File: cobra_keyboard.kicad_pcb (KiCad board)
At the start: 2 copper layers, 298.4 x 116.8 mm, 93 parts, among them K100 DOWN, K101 UP, K102 SPACE, K103 LEFT, K104 RIGHT, K200 CTRL, K201 CS, K202 Z, K203 X, K204 C, K205 V, K206 B, K207 N, K208 M, K209 NEW M, K210 SS, K211 F4, K300 NO SCR, K301 CS LK, K302 GRAPH, K303 A, K304 S, K305 D, K306 F, K307 G, K308 H, K309 J, K310 K, K311 L, K312 ENTER, K313 F3, K400 LF, K401 TAB, K402 Q, K403 W, K404 E, K405 R, K406 T, K407 Y, K408 U, K409 I, K410 O, K411 P, K412 F2, K500 ESC, K501 PG ED, K502 1, K503 2, K504 3, K505 4, K506 5, K507 6, K508 7, K509 8, K510 9, K511 0, K512 DEL, K513 F1, T201 BC337, T210 BC337, T411 BC337, T502 BC337, T503 BC337, T506 BC337, T507 BC337, T508 BC337, T509 BC337, T510 BC337, T511 BC337

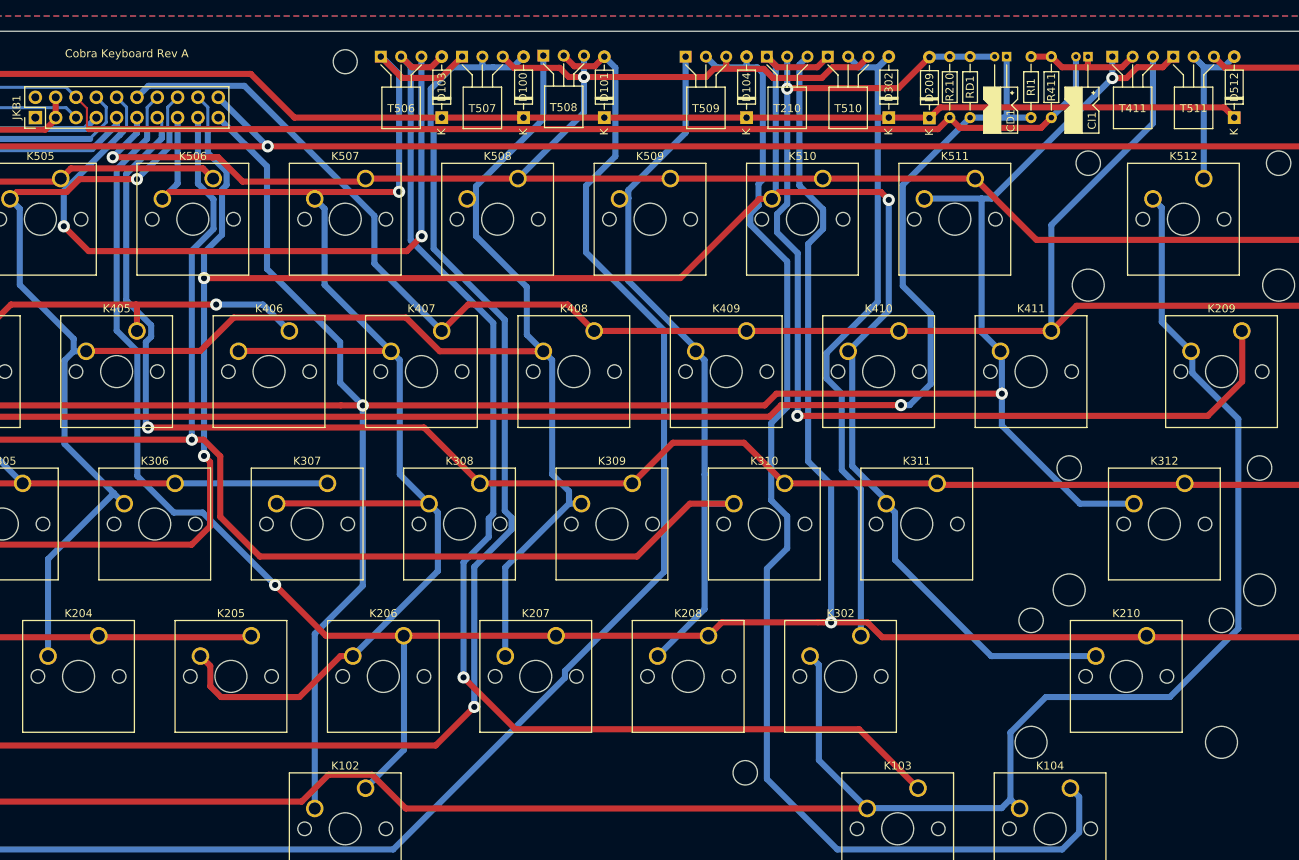
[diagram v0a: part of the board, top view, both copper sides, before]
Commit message: Swap GRAPH and NEW MODE keys
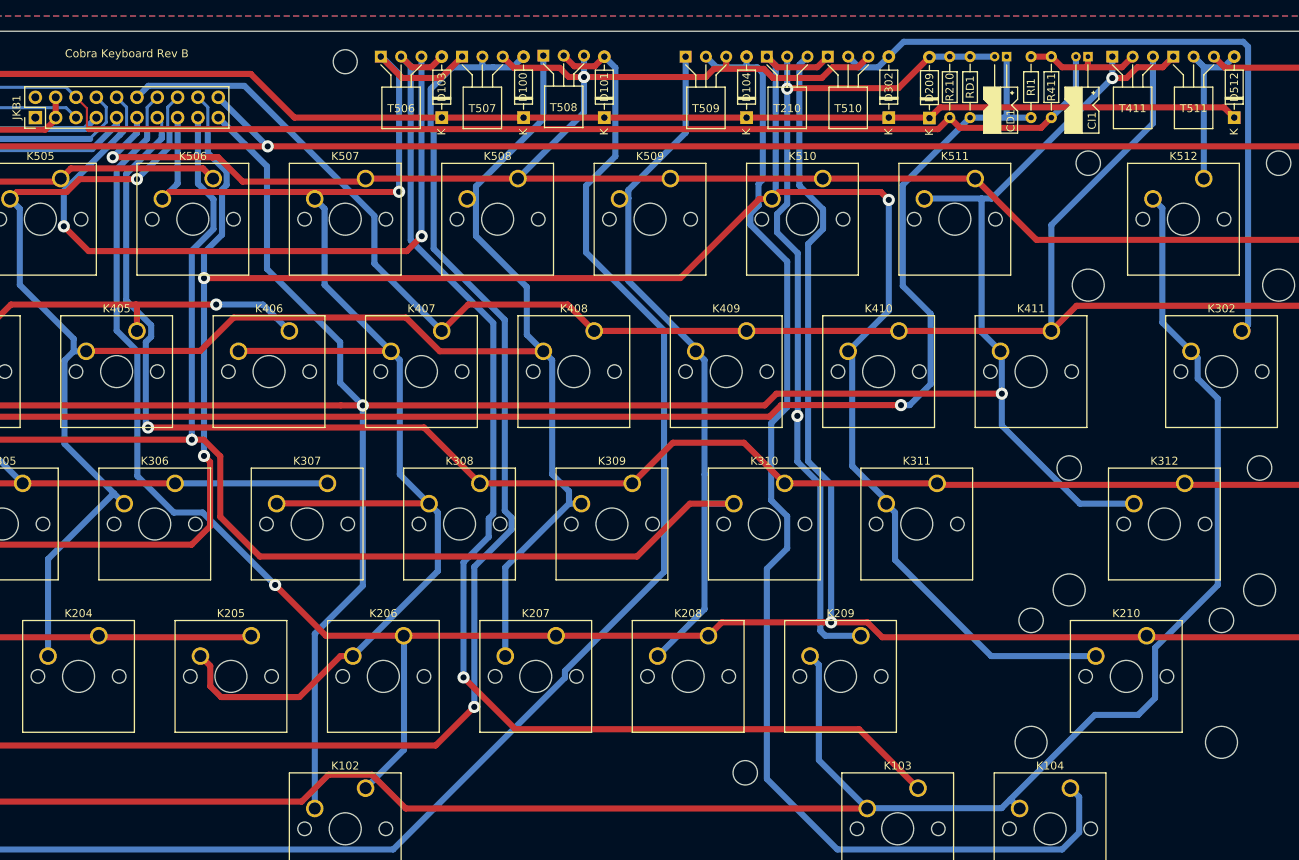
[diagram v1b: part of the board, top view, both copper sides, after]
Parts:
- K209: footprint Button_Switch_Keyboard:SW_Cherry_MX_1.50u_PCB -> Button_Switch_Keyboard:SW_Cherry_MX_1.00u_PCB
- K302: footprint Button_Switch_Keyboard:SW_Cherry_MX_1.00u_PCB -> Button_Switch_Keyboard:SW_Cherry_MX_1.50u_PCB
- moved K209 61.0 mm to (213.7, 75.6)
- moved K302 61.0 mm to (261.3, 37.5)
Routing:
- net Net-(CD1-Pad2): track 137.8 -> 107.5 mm
- net Net-(K100-Pad2): track 432.5 -> 424.4 mm
- net Net-(D302-Pad2): track 83.6 -> 88.0 mm
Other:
- board text added: "Cobra Keyboard Rev B"
- board text removed: "Cobra Keyboard Rev A"
